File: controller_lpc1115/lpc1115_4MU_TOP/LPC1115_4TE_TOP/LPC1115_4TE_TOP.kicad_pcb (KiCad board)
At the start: 2 copper layers, 67 x 42 mm, 101 parts, among them P1 ML26, P2 ISP, P3 FE12-1, Q1 BC856, Q2 FZT753, Q3 BC847, U1 LPC1115FBD48, U2 BD9G101, U3 12MHz

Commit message: update all stuff
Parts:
- removed U3: 12MHz, Oscillator:Oscillator_SMD_EuroQuartz_XO32-4Pin_3.2x2.5mm
- added D10: 1N4148W, Diode_SMD:D_SOD-123, B.Cu at (130.8, 86.4)
- added R3: 390k, Resistor_SMD:R_0805_2012Metric, B.Cu at (126.5, 94.5)
- added R4: 43k, Resistor_SMD:R_0805_2012Metric, B.Cu at (123.7, 93.6)
- added X1: 12MHz, Oscillator:Oscillator_SMD_EuroQuartz_XO32-4Pin_3.2x2.5mm, B.Cu at (140.4, 112.2)
- C1: value 15nF -> 15n
- C10, C11, C14, C21, C5, C8: value 100nF -> 100n
- C13, C24: value 1uF -> 1u
- C15, C18: value 100pF -> 100p
- C16, C17, C19: value 10nF -> 10n
- C2: value 470n -> 270n
- C22: value 220pF -> 220p
- C23: moved to F.Cu
- C3: value VF 100/35 K-D8 -> 100µ/35V
- C4: value 4.7uF 50V -> 4.7µ/50V
- C6: value 47uF 10V -> 47µ/10V
- C7: value 100uF -> 100µ/10V
- D1, D11, D12, D14, D17, D2, D3, D4, D5, D6, D7, D8: value CD4148W -> 1N4148W; footprint Diode_SMD:D_0805_2012Metric -> Diode_SMD:D_SOD-123
- D13: value SMAJ40AC -> SMAJ40CA
- D15, D16: footprint Diode_SMD:D_SOD-123 -> Diode_SMD:D_MiniMELF
- L1: value 4.7uH -> 10u
- R1: value 24R 2512 1.0W -> 24R 1W
- R17: value 6,2k -> 6k2
- R2: value 1k6 -> 88k7
- R5: value 470R -> 22k1
- U1: value LPC1115FBD48 -> LPC1115FBD48-303
- U2: value BD9G101 -> TPS560430
- moved C23 16.7 mm to (150.9, 112.0), turned to 180 degrees
- moved R23 5.36 mm to (162.3, 85.9), turned to 180 degrees
- moved R20 2.20 mm to (157.7, 89.2)
- moved D11 2.12 mm to (161.8, 90.7)
- moved D17 1.70 mm to (161.8, 88.1)
- moved D14 0.96 mm to (161.8, 93.2)
- moved JP1 0.75 mm to (143.4, 98.3), turned to 0 degrees
- moved D12 0.40 mm to (144.5, 95.5)
- moved R1 0.33 mm to (154.2, 89.7)
- moved D8 0.33 mm to (141.0, 115.0)
- moved D1 0.25 mm to (129.8, 94.7)
- moved D16 0.07 mm to (149.6, 93.5)
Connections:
- U2 pad 4: /EIB_DC -> Net-(U2-EN)
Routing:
- net Net-(U2-EN): track 0.00 -> 8.79 mm, vias 0 -> 2
- net +3V3: track 245.5 -> 254.0 mm, vias 10 -> 11
- net Net-(D17-K): track 34.5 -> 39.1 mm
- net Net-(D10-K): track 1.96 -> 5.67 mm
- net /EIB_IN: track 20.5 -> 22.7 mm
- net Net-(D1-A): track 8.43 -> 10.2 mm
- net Net-(JP1-B): track 26.1 -> 24.5 mm
- net Net-(SJ1-C): track 51.4 -> 50.1 mm
- net /LT1: track 89.3 -> 90.5 mm
- net /IO5: track 29.3 -> 30.5 mm
- net /LT9: track 113.8 -> 114.9 mm
- net /LT7: track 24.0 -> 22.8 mm
- net /EIB+: track 15.2 -> 16.3 mm
- net Net-(D11-K): track 8.30 -> 7.16 mm
- net Net-(D8-A): track 16.0 -> 17.1 mm
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
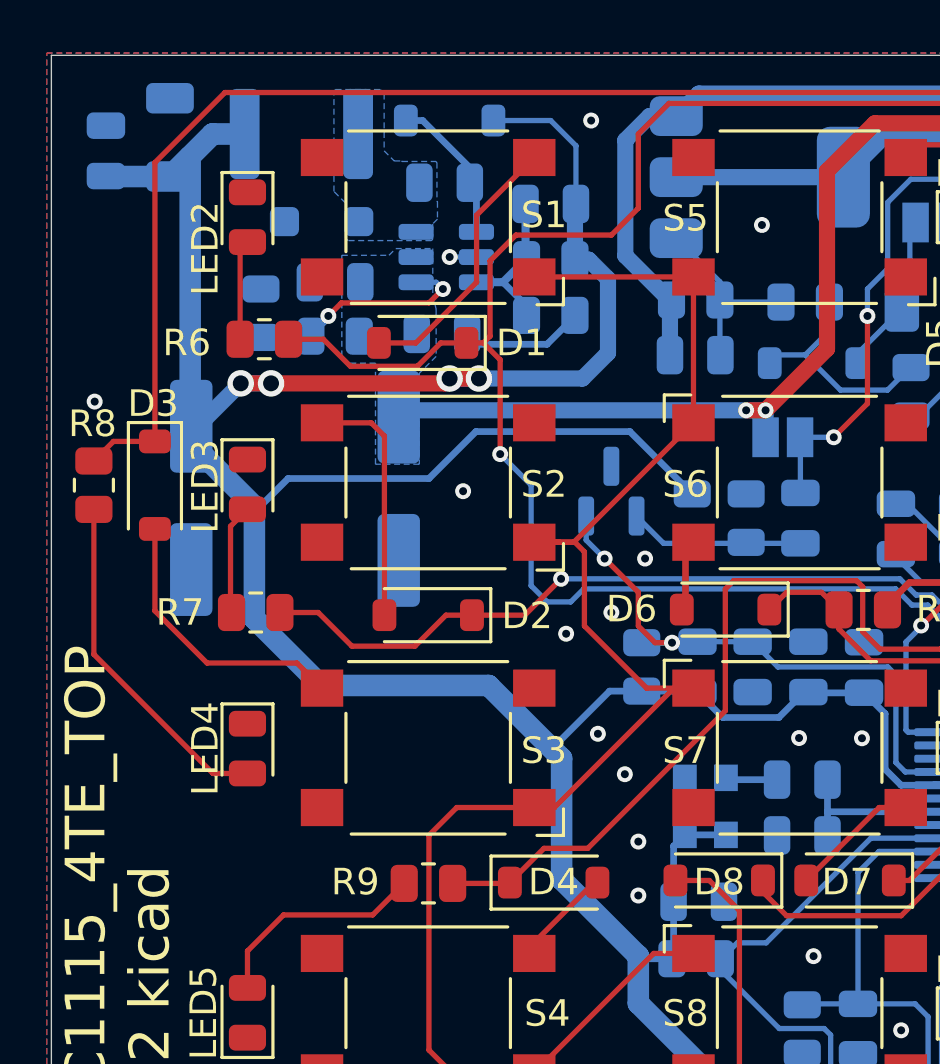
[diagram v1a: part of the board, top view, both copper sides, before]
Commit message: fixups for 2MU/4MU controllers - use Seiko oszillator
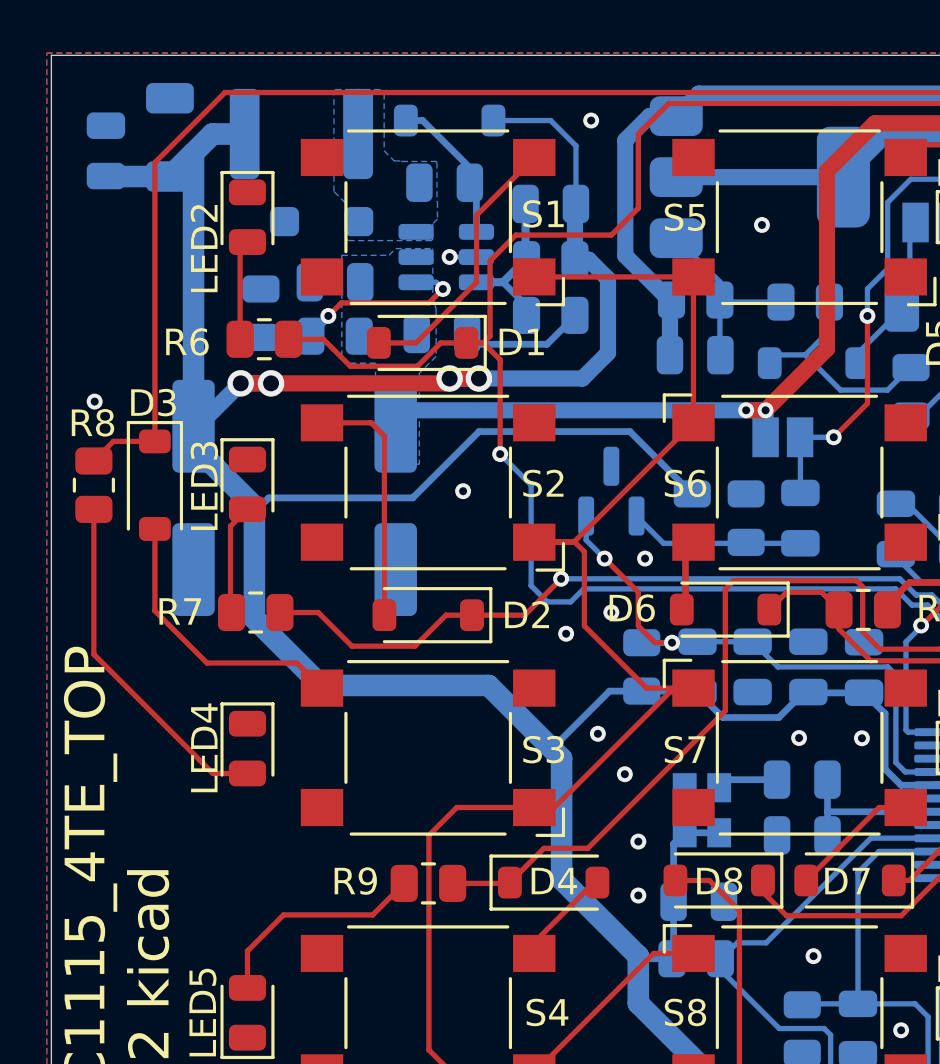
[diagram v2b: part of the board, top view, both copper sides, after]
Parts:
- C4: value 4.7µ/50V -> 4.7µ/35V
- X1: footprint Oscillator:Oscillator_SMD_EuroQuartz_XO32-4Pin_3.2x2.5mm -> Oscillator:Oscillator_SMD_SeikoEpson_SG210-4Pin_2.5x2.0mm
- moved C3 0.36 mm to (128.8, 100.6)
- moved X1 0.20 mm to (140.3, 112.4), turned to 90 degrees
- moved C7 0.09 mm to (121.2, 100.6)
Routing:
- net +3V3: vias 11 -> 12
- net GND: vias 41 -> 40

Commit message: finally standardize selected parts on all boards
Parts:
- C12, C23: value 100nF -> 100n
- C3: value 100µ/35V -> 100u/35V
- C4: value 4.7µ/35V -> 4.7u/35V
- C6: value 47µ/10V -> 47u/10V
- C7: value 100µ/10V -> 100u/10V
- C9: value 10nF -> 10n
- D9: footprint Diode_SMD:D_SOD-123F -> Diode_SMD:D_SOD-123
- P3: footprint Connector_PinSocket_2.54mm:PinSocket_1x12_P2.54mm_Vertical -> Connector_PinHeader_2.54mm:PinHeader_1x12_P2.54mm_Vertical
- moved D9 0.25 mm to (125.7, 90.2)
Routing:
- net GND: vias 40 -> 41
- net +3V3: vias 12 -> 11
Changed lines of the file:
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@@
 		)
 	)
-	(footprint "Connector_PinSocket_2.54mm:PinSocket_1x12_P2.54mm_Vertical"
+	(footprint "Connector_PinHeader_2.54mm:PinHeader_1x12_P2.54mm_Vertical"
 		(layer "F.Cu")
 		(at 168.402 121.666 180)
-		(descr "Through hole straight socket strip, 1x12, 2.54mm pitch, single row (from Kicad 4.0.7), script generated")
-		(tags "Through hole socket strip THT 1x12 2.54mm single row")
+		(descr "Through hole straight pin header, 1x12, 2.54mm pitch, single row")
+		(tags "Through hole pin header THT 1x12 2.54mm single row")
 		(property "Reference" "P3"
-			(at 0 -2.77 180)
+			(at 0 -2.33 180)
 			(layer "F.SilkS")
 			(effects
@@
 		)
 		(property "Value" "FE12-1"
-			(at 0 30.71 180)
+			(at 0 30.27 180)
 			(layer "F.Fab")
 			(effects
@@
 			)
 		)
-		(property "Footprint" "Connector_PinSocket_2.54mm:PinSocket_1x12_P2.54mm_Vertical"
+		(property "Footprint" "Connector_PinHeader_2.54mm:PinHeader_1x12_P2.54mm_Vertical"
 			(at 0 0 180)
 			(unlocked yes)
@@
 		(sheetname "Stammblatt")
 		(sheetfile "LPC1115_4TE_TOP.kicad_sch")
-		(attr through_hole dnp)
+		(attr through_hole exclude_from_bom dnp)
 		(fp_line
 			(start 1.33 1.27)
@@
 		)
 		(fp_line
-			(start 1.33 -1.33)
-			(end 1.33 0)
+			(start -1.33 29.27)
+			(end 1.33 29.27)
 			(stroke
 				(width 0.12)
@@
 		)
 		(fp_line
-			(start 0 -1.33)
-			(end 1.33 -1.33)
+			(start -1.33 1.27)
+			(end 1.33 1.27)
 			(stroke
 				(width 0.12)
@@
 		)
 		(fp_line
-			(start -1.33 29.27)
-			(end 1.33 29.27)
+			(start -1.33 1.27)
+			(end -1.33 29.27)
 			(stroke
 				(width 0.12)
@@
 		)
 		(fp_line
-			(start -1.33 1.27)
-			(end 1.33 1.27)
+			(start -1.33 0)
+			(end -1.33 -1.33)
 			(stroke
 				(width 0.12)
@@
 		)
 		(fp_line
-			(start -1.33 1.27)
-			(end -1.33 29.27)
+			(start -1.33 -1.33)
+			(end 0 -1.33)
 			(stroke
 				(width 0.12)
@@
 		)
 		(fp_line
-			(start 1.75 29.7)
-			(end -1.8 29.7)
+			(start 1.8 29.75)
+			(end 1.8 -1.8)
 			(stroke
 				(width 0.05)
@@
 		)
 		(fp_line
-			(start 1.75 -1.8)
-			(end 1.75 29.7)
+			(start 1.8 -1.8)
+			(end -1.8 -1.8)
 			(stroke
 				(width 0.05)
@@
 		)
 		(fp_line
-			(start -1.8 29.7)
-			(end -1.8 -1.8)
+			(start -1.8 29.75)
+			(end 1.8 29.75)
 			(stroke
 				(width 0.05)
@@
 		(fp_line
 			(start -1.8 -1.8)
-			(end 1.75 -1.8)
+			(end -1.8 29.75)
 			(stroke
 				(width 0.05)
@@
 		)
 		(fp_line
-			(start 1.27 -0.635)
+			(start 1.27 -1.27)
 			(end 1.27 29.21)
 			(stroke
@@
 		)
 		(fp_line
-			(start 0.635 -1.27)
-			(end 1.27 -0.635)
+			(start -0.635 -1.27)
+			(end 1.27 -1.27)
 			(stroke
 				(width 0.1)
@@
 		(fp_line
 			(start -1.27 29.21)
-			(end -1.27 -1.27)
+			(end -1.27 -0.635)
 			(stroke
 				(width 0.1)
@@
 		)
 		(fp_line
-			(start -1.27 -1.27)
-			(end 0.635 -1.27)
+			(start -1.27 -0.635)
+			(end -0.635 -1.27)
 			(stroke
 				(width 0.1)
@@
 			(pintype "passive")
 		)
-		(model "${KICAD8_3DMODEL_DIR}/Connector_PinSocket_2.54mm.3dshapes/PinSocket_1x12_P2.54mm_Vertical.wrl"
+		(model "${KICAD8_3DMODEL_DIR}/Connector_PinHeader_2.54mm.3dshapes/PinHeader_1x12_P2.54mm_Vertical.wrl"
 			(offset
 				(xyz 0 0 0)
@@
 			)
 		)
-		(property "Value" "100nF"
+		(property "Value" "100n"
 			(at 0 1.68 0)
 			(layer "F.Fab")
@@
 		)
 	)
-	(footprint "Diode_SMD:D_SOD-123F"
+	(footprint "Diode_SMD:D_SOD-123"
 		(layer "B.Cu")
-		(at 125.984 90.17 180)
-		(descr "D_SOD-123F")
-		(tags "D_SOD-123F")
+		(at 125.73 90.17 180)
+		(descr "SOD-123")
+		(tags "SOD-123")
 		(property "Reference" "D9"
-			(at 3.302 -0.762 180)
+			(at 3.302 -0.762 0)
 			(layer "B.SilkS")
 			(effects
@@
 		)
 		(property "Value" "RB060M-60 / MBR 140SFT1G"
-			(at 0 -2.1 180)
+			(at 0 -2.1 0)
 			(layer "B.Fab")
 			(effects
@@
 			)
 		)
-		(property "Footprint" "Diode_SMD:D_SOD-123F"
+		(property "Footprint" "Diode_SMD:D_SOD-123"
 			(at 0 0 0)
 			(unlocked yes)
@@
 		(fp_line
 			(start 1.65 1)
-			(end -2.21 1)
+			(end -2.36 1)
 			(stroke
 				(width 0.12)
@@
 		(fp_line
 			(start 1.65 -1)
-			(end -2.21 -1)
+			(end -2.36 -1)
 			(stroke
 				(width 0.12)
@@
 		)
 		(fp_line
-			(start -2.21 -1)
-			(end -2.21 1)
+			(start -2.36 -1)
+			(end -2.36 1)
 			(stroke
 				(width 0.12)
@@
 		)
 		(fp_line
-			(start 2.2 1.15)
-			(end -2.2 1.15)
+			(start 2.35 1.15)
+			(end -2.35 1.15)
 			(stroke
 				(width 0.05)
@@
 		)
 		(fp_line
-			(start 2.2 -1.15)
-			(end 2.2 1.15)
+			(start 2.35 -1.15)
+			(end 2.35 1.15)
 			(stroke
 				(width 0.05)
@@
 		)
 		(fp_line
-			(start -2.2 -1.15)
-			(end 2.2 -1.15)
+			(start -2.35 -1.15)
+			(end 2.35 -1.15)
 			(stroke
 				(width 0.05)
@@
 		)
 		(fp_line
-			(start -2.2 -1.15)
-			(end -2.2 1.15)
+			(start -2.35 -1.15)
+			(end -2.35 1.15)
 			(stroke
 				(width 0.05)
@@
 		)
 		(fp_text user "${REFERENCE}"
-			(at -0.127 1.905 180)
+			(at 0 2 0)
 			(layer "B.Fab")
 			(effects
@@
 		)
 		(pad "1" smd roundrect
-			(at -1.4 0 180)
-			(size 1.1 1.1)
+			(at -1.65 0 180)
+			(size 0.9 1.2)
 			(layers "B.Cu" "B.Paste" "B.Mask")
-			(roundrect_rratio 0.2272727273)
+			(roundrect_rratio 0.25)
 			(net 52 "Net-(D9-K)")
 			(pinfunction "K")
@@
 		)
 		(pad "2" smd roundrect
-			(at 1.4 0 180)
-			(size 1.1 1.1)
+			(at 1.65 0 180)
+			(size 0.9 1.2)
 			(layers "B.Cu" "B.Paste" "B.Mask")
-			(roundrect_rratio 0.2272727273)
+			(roundrect_rratio 0.25)
 			(net 3 "GND")
 			(pinfunction "A")
 			(pintype "passive")
 		)
-		(model "${KICAD8_3DMODEL_DIR}/Diode_SMD.3dshapes/D_SOD-123F.wrl"
+		(model "${KICAD8_3DMODEL_DIR}/Diode_SMD.3dshapes/D_SOD-123.wrl"
 			(offset
 				(xyz 0 0 0)
@@
 			)
 		)
-		(property "Value" "100µ/35V"
+		(property "Value" "100u/35V"
 			(at 0 -4.35 90)
 			(layer "B.Fab")
@@
 		(sheetname "Stammblatt")
 		(sheetfile "LPC1115_4TE_TOP.kicad_sch")
-		(attr smd dnp)
+		(attr smd exclude_from_bom dnp)
 		(fp_line
 			(start 2 -1.65)
@@
 			)
 		)
-		(property "Value" "100nF"
+		(property "Value" "100n"
 			(at 0 -1.68 90)
 			(layer "B.Fab")
@@
 		)
 		(property "Value" "12MHz"
-			(at 0 -2.2 270)
+			(at 0 -2.2 -90)
 			(layer "B.Fab")
 			(effects
@@
 				(font
 					(size 1.27 1.27)
+					(thickness 0.15)
 				)
 				(justify mirror)
@@
 				(font
 					(size 1.27 1.27)
+					(thickness 0.15)
 				)
 				(justify mirror)
@@
 				(font
 					(size 1.27 1.27)
+					(thickness 0.15)
 				)
 				(justify mirror)
@@
 		)
 		(fp_text user "${REFERENCE}"
-			(at 0 0 270)
+			(at 0 0 -90)
 			(layer "B.Fab")
 			(effects
@@
 			)
 		)
-		(property "Value" "100µ/10V"
+		(property "Value" "100u/10V"
 			(at 0 -4.35 90)
 			(layer "B.Fab")
@@
 		(sheetname "Stammblatt")
 		(sheetfile "LPC1115_4TE_TOP.kicad_sch")
-		(attr smd dnp)
+		(attr smd exclude_from_bom dnp)
 		(fp_line
 			(start 0.261252 0.735)
@@
 		(tags "inductor")
 		(property "Reference" "L1"
-			(at 2.54 -2.794 180)
+			(at 2.794 -2.794 180)
 			(layer "B.SilkS")
 			(effects
@@
 			)
 		)
-		(property "Value" "47µ/10V"
+		(property "Value" "47u/10V"
 			(at 0 -1.85 -90)
 			(layer "B.Fab")
@@
 		(sheetname "Stammblatt")
 		(sheetfile "LPC1115_4TE_TOP.kicad_sch")
-		(attr smd dnp)
+		(attr smd exclude_from_bom dnp)
 		(fp_line
 			(start -2.36 -1)
@@
 			)
 		)
-		(property "Value" "10nF"
+		(property "Value" "10n"
 			(at 0 -1.68 90)
 			(layer "B.Fab")
@@
 			)
 		)
-		(property "Value" "4.7µ/35V"
+		(property "Value" "4.7u/35V"
 			(at 0 -1.68 180)
 			(layer "B.Fab")
@@
 	)
 	(via
+		(at 137.668 110.744)
+		(size 0.6)
+		(drill 0.3)
+		(layers "F.Cu" "B.Cu")
+		(net 3)
+	)
+	(via
 		(at 150.368 121.539)
 		(size 0.6)
@@
 		(net 11)
 	)
-	(via
-		(at 137.414 110.998)
-		(size 0.6)
-		(drill 0.3)
-		(layers "F.Cu" "B.Cu")
-		(net 11)
-	)

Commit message: final for manufacturing
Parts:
- R10, R11, R12, R13, R27, R28, R6, R7, R8, R9: value 1k5 -> 1k
- R2: value 88k7 -> 51k
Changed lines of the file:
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@@
 			)
 		)
-		(property "Value" "1k5"
+		(property "Value" "1k"
 			(at 0 1.65 0)
 			(layer "F.Fab")
@@
 			)
 		)
-		(property "Value" "1k5"
+		(property "Value" "1k"
 			(at 0 1.65 -90)
 			(layer "F.Fab")
@@
 			)
 		)
-		(property "Value" "1k5"
+		(property "Value" "1k"
 			(at 0 1.65 0)
 			(layer "F.Fab")
@@
 			)
 		)
-		(property "Value" "1k5"
+		(property "Value" "1k"
 			(at 0 1.65 -90)
 			(layer "F.Fab")
@@
 			)
 		)
-		(property "Value" "1k5"
+		(property "Value" "1k"
 			(at 0 1.65 0)
 			(layer "F.Fab")
@@
 			)
 		)
-		(property "Value" "1k5"
+		(property "Value" "1k"
 			(at 0 1.65 180)
 			(layer "F.Fab")
@@
 			)
 		)
-		(property "Value" "1k5"
+		(property "Value" "1k"
 			(at 0 1.65 0)
 			(layer "F.Fab")
@@
 			)
 		)
-		(property "Value" "1k5"
+		(property "Value" "1k"
 			(at 0 1.65 0)
 			(layer "F.Fab")
@@
 			)
 		)
-		(property "Value" "1k5"
+		(property "Value" "1k"
 			(at 0 1.65 180)
 			(layer "F.Fab")
@@
 			)
 		)
-		(property "Value" "1k5"
+		(property "Value" "1k"
 			(at 0 1.65 90)
 			(layer "F.Fab")
@@
 			)
 		)
-		(property "Value" "88k7"
+		(property "Value" "51k"
 			(at 0 -1.65 0)
 			(layer "B.Fab")

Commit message: update LPC1115_4TE_TOP
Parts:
- C1: value 15n -> 100n
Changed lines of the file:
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@@
 			)
 		)
-		(property "Value" "15n"
+		(property "Value" "100n"
 			(at 0 -1.68 0)
 			(layer "B.Fab")

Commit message: controllers: reduce osc load, fix DNP for voltage measurement
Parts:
- C18: value 100p -> 22p
- C22: value 220p -> 22p
- R21: value 47k -> 100k
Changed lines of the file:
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@@
 			)
 		)
-		(property "Value" "220p"
+		(property "Value" "22p"
 			(at 0 -1.68 180)
 			(layer "B.Fab")
@@
 			)
 		)
-		(property "Value" "100p"
+		(property "Value" "22p"
 			(at 0 -1.68 0)
 			(layer "B.Fab")
@@
 			)
 		)
-		(property "Value" "47k"
+		(property "Value" "100k"
 			(at 0 -1.65 -90)
 			(layer "B.Fab")
@@
 		(sheetname "Stammblatt")
 		(sheetfile "LPC1115_4TE_TOP.kicad_sch")
-		(attr smd)
+		(attr smd exclude_from_bom dnp)
 		(fp_line
 			(start 0.261252 0.735)
